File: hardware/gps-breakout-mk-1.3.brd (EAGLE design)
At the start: 17.8 x 22.9 mm, 10 parts

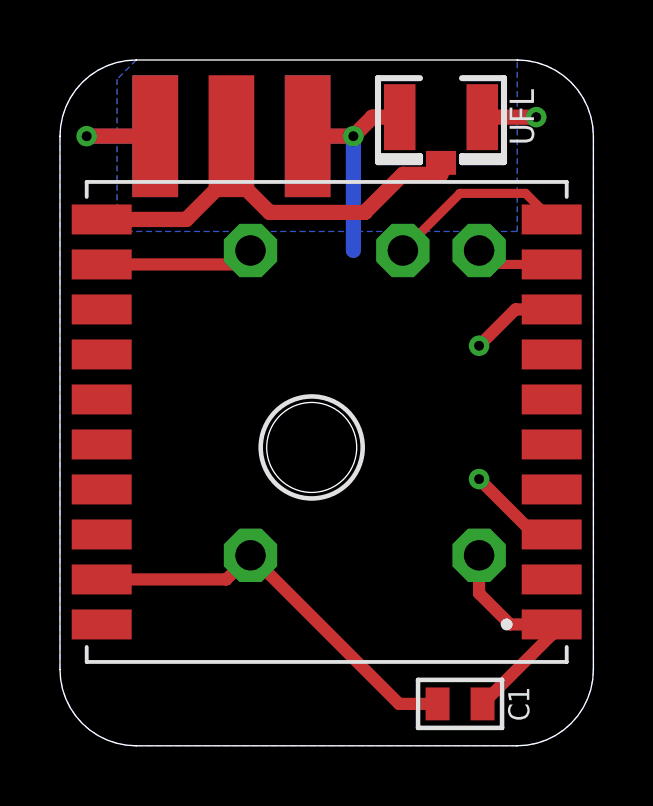
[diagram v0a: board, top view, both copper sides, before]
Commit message: change to gps module again: the rest of it
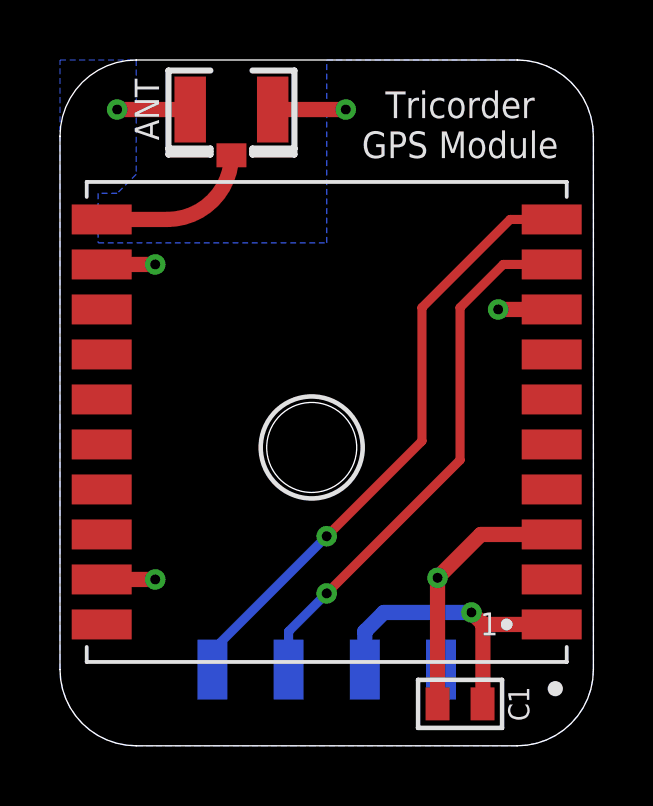
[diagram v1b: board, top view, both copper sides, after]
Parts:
- removed 3V, GND, GND2, RX, TX: M01PTH-1MM, a_parts:1X01-1MM-NS
- removed SMA: (no value), a_parts:SMA-EDGE
- removed UFL: (no value), a_parts:U.FL
- added ANT: (no value), a_parts:U.FL
- added JP2: M04SMD-FEMALE, a_parts:1X04-SMD-FEMALE-RA
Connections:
- net 3.3V: now also JP2.P$2; no longer 3V.1
- net GND: now also ANT.1, ANT.2, JP2.P$1; no longer GND.1, GND2.1, SMA.GND@0, SMA.GND@1, SMA.GND@2, SMA.GND@3, UFL.1, UFL.2
- net GPS_RX: now also JP2.P$4; no longer RX.1
- net GPS_TX: now also JP2.P$3; no longer TX.1
- net N$1: now also ANT.3; no longer SMA.SIG, UFL.3
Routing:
- net GND: track 39.9 -> 18.8 mm, vias 5 -> 6
- net GPS_TX: track 2.61 -> 18.1 mm, vias 0 -> 1
- net GPS_RX: track 6.11 -> 20.5 mm, vias 0 -> 1
- net N$1: track 14.6 -> 5.21 mm
- net 3.3V: track 7.72 -> 10.6 mm, vias 0 -> 1
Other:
- board text added: "1"
- board text added: "RX"
- board text added: "TX"
- board text added: "VCC"
